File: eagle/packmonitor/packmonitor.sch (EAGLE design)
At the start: 29 parts, among them IC1 24C64, IC2 TCA4311A, IC3 AVRXDA32TQFP, IC4 ACS712

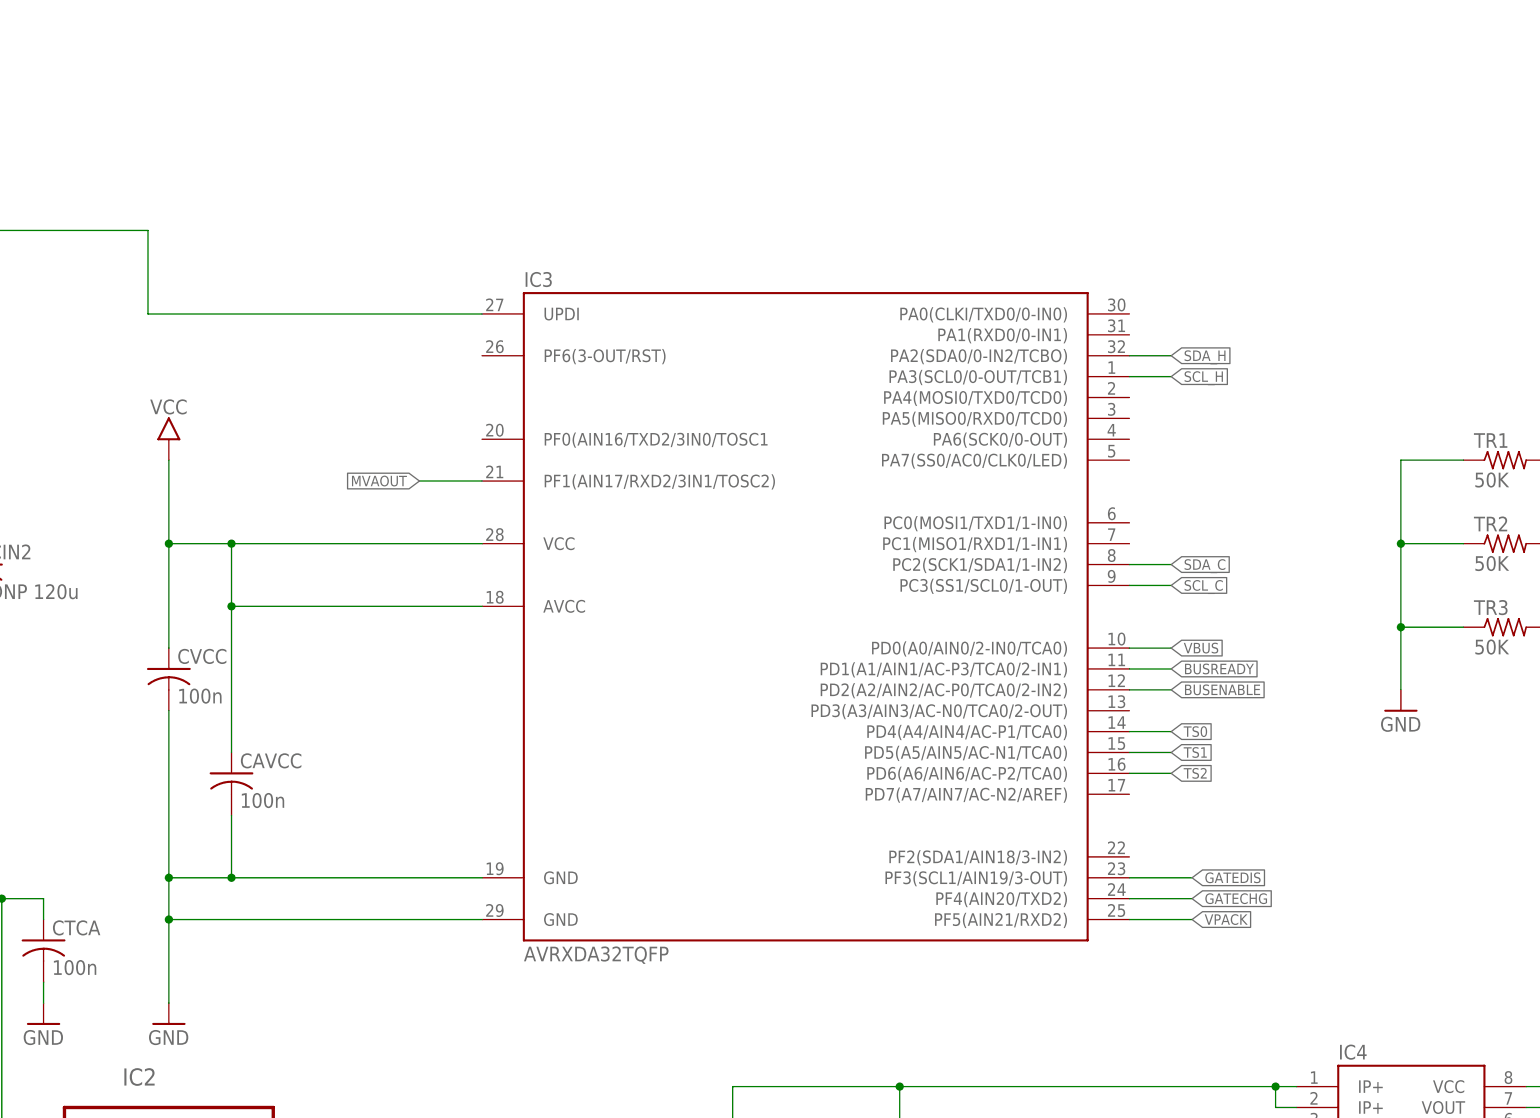
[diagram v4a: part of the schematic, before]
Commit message: Added pull up resistors on i2c busses
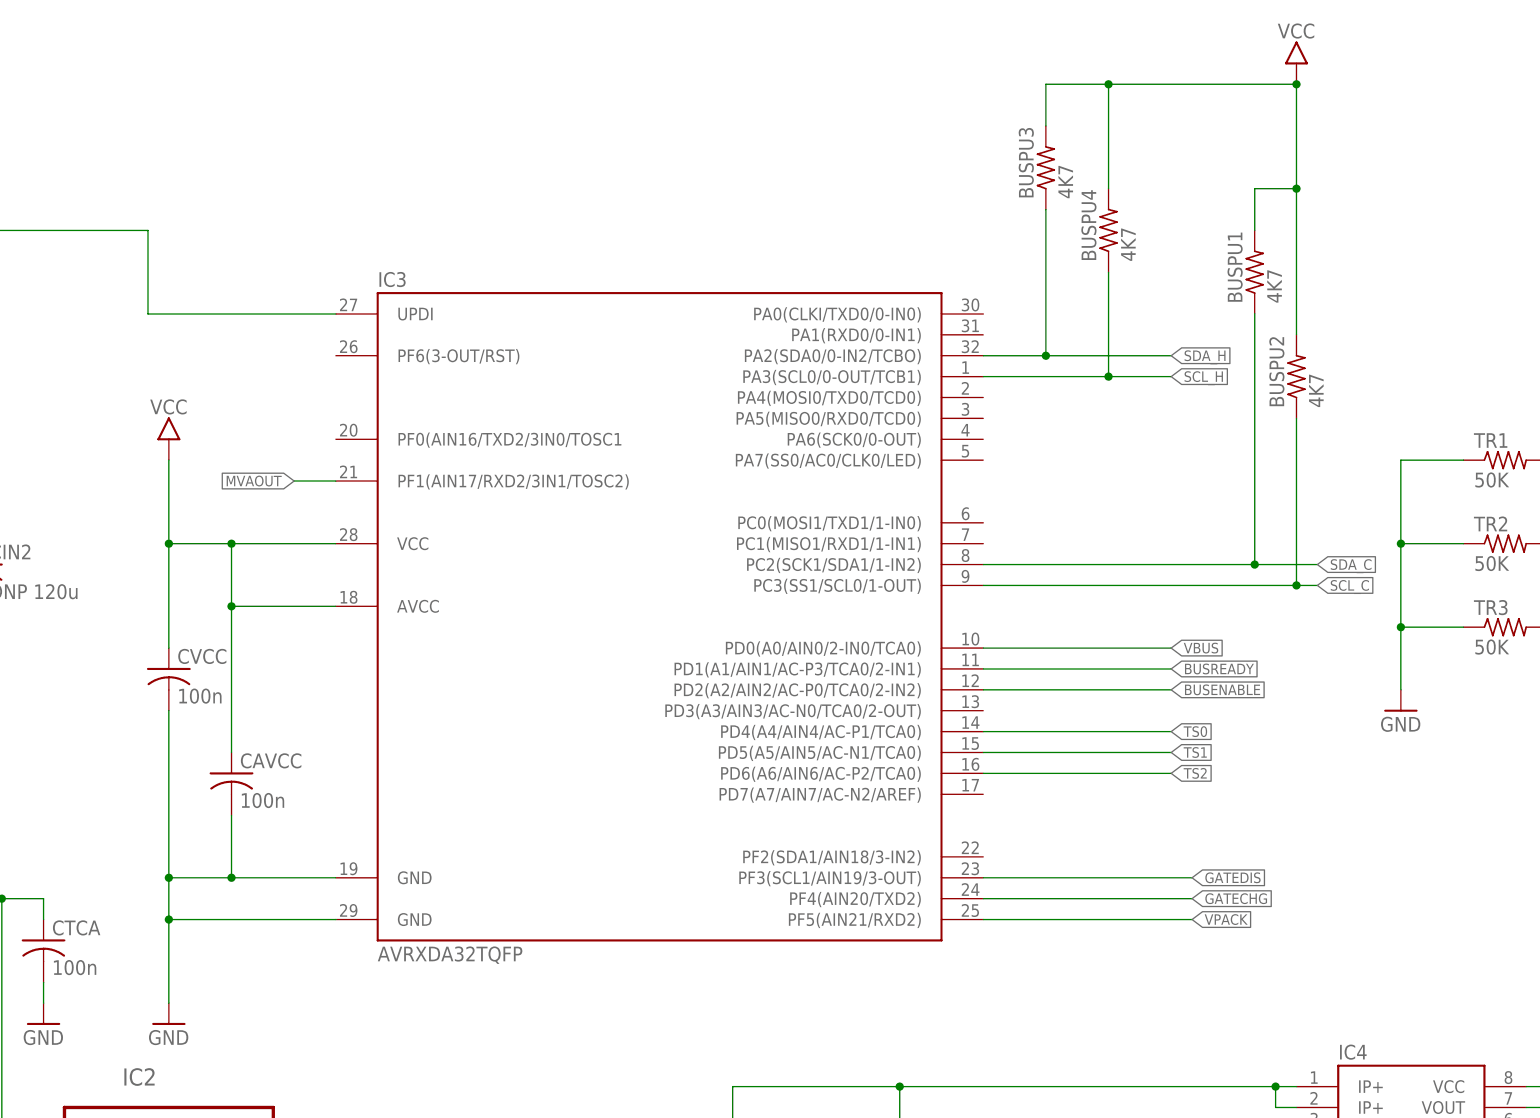
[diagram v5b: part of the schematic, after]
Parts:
- added BUSPU1, BUSPU2, BUSPU3, BUSPU4: 4K7, rcl:R-US_R0603
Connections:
- net SCL_C: now also BUSPU2.1
- net SCL_H: now also BUSPU4.1
- net SDA_C: now also BUSPU1.1
- net SDA_H: now also BUSPU3.1
- net VCC: now also BUSPU1.2, BUSPU2.2, BUSPU3.2, BUSPU4.2
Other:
- moved on the sheet: IC3
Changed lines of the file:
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@@
 <part name="RENA" library="rcl" deviceset="R-US_" device="R0603" value="10K"/>
 <part name="CACS1" library="rcl" deviceset="C-US" device="C0603" value="1n"/>
+<part name="BUSPU1" library="rcl" deviceset="R-US_" device="R0603" value="4K7"/>
+<part name="BUSPU2" library="rcl" deviceset="R-US_" device="R0603" value="4K7"/>
+<part name="U$4" library="bt" deviceset="VCC" device=""/>
+<part name="BUSPU3" library="rcl" deviceset="R-US_" device="R0603" value="4K7"/>
+<part name="BUSPU4" library="rcl" deviceset="R-US_" device="R0603" value="4K7"/>
 </parts>
 <sheets>
@@
 <instance part="CACS2" gate="G$1" x="180.34" y="88.9"/>
 <instance part="CIN1" gate="G$1" x="-45.72" y="154.94"/>
-<instance part="IC3" gate="G$1" x="71.12" y="147.32"/>
+<instance part="IC3" gate="G$1" x="53.34" y="147.32"/>
 <instance part="QCHG" gate="G$1" x="111.76" y="35.56" rot="R270"/>
 <instance part="QDIS" gate="G$1" x="127" y="35.56" rot="MR270"/>
@@
 <instance part="RENA" gate="G$1" x="-33.02" y="55.88" rot="R90"/>
 <instance part="CACS1" gate="G$1" x="172.72" y="73.66"/>
+<instance part="BUSPU1" gate="G$1" x="124.46" y="190.5" rot="R90"/>
+<instance part="BUSPU2" gate="G$1" x="129.54" y="177.8" rot="R90"/>
+<instance part="U$4" gate="G$1" x="129.54" y="213.36"/>
+<instance part="BUSPU3" gate="G$1" x="99.06" y="203.2" rot="R90"/>
+<instance part="BUSPU4" gate="G$1" x="106.68" y="195.58" rot="R90"/>
 </instances>
 <busses>
@@
 <segment>
 <pinref part="U$2" gate="G$1" pin="VCC"/>
-<wire x1="30.48" y1="157.48" x2="0" y2="157.48" width="0.1524" layer="91"/>
+<wire x1="12.7" y1="157.48" x2="0" y2="157.48" width="0.1524" layer="91"/>
 <wire x1="0" y1="157.48" x2="-7.62" y2="157.48" width="0.1524" layer="91"/>
 <wire x1="-7.62" y1="157.48" x2="-7.62" y2="167.64" width="0.1524" layer="91"/>
@@
 <junction x="-7.62" y="157.48"/>
 <pinref part="CAVCC" gate="G$1" pin="1"/>
-<wire x1="30.48" y1="149.86" x2="0" y2="149.86" width="0.1524" layer="91"/>
+<wire x1="12.7" y1="149.86" x2="0" y2="149.86" width="0.1524" layer="91"/>
 <wire x1="0" y1="149.86" x2="0" y2="132.08" width="0.1524" layer="91"/>
 <wire x1="0" y1="149.86" x2="0" y2="157.48" width="0.1524" layer="91"/>
@@
 <junction x="162.56" y="93.98"/>
 </segment>
+<segment>
+<pinref part="BUSPU2" gate="G$1" pin="2"/>
+<wire x1="129.54" y1="182.88" x2="129.54" y2="200.66" width="0.1524" layer="91"/>
+<pinref part="BUSPU1" gate="G$1" pin="2"/>
+<wire x1="129.54" y1="200.66" x2="124.46" y2="200.66" width="0.1524" layer="91"/>
+<wire x1="124.46" y1="200.66" x2="124.46" y2="195.58" width="0.1524" layer="91"/>
+<wire x1="129.54" y1="200.66" x2="129.54" y2="213.36" width="0.1524" layer="91"/>
+<junction x="129.54" y="200.66"/>
+<pinref part="U$4" gate="G$1" pin="VCC"/>
+<pinref part="BUSPU3" gate="G$1" pin="2"/>
+<wire x1="99.06" y1="208.28" x2="99.06" y2="213.36" width="0.1524" layer="91"/>
+<wire x1="99.06" y1="213.36" x2="106.68" y2="213.36" width="0.1524" layer="91"/>
+<junction x="129.54" y="213.36"/>
+<pinref part="BUSPU4" gate="G$1" pin="2"/>
+<wire x1="106.68" y1="213.36" x2="129.54" y2="213.36" width="0.1524" layer="91"/>
+<wire x1="106.68" y1="200.66" x2="106.68" y2="213.36" width="0.1524" layer="91"/>
+<junction x="106.68" y="213.36"/>
+</segment>
 </net>
 <net name="GND" class="0">
@@
 <wire x1="-7.62" y1="116.84" x2="-7.62" y2="111.76" width="0.1524" layer="91"/>
 <wire x1="-7.62" y1="111.76" x2="-7.62" y2="101.6" width="0.1524" layer="91"/>
-<wire x1="30.48" y1="111.76" x2="-7.62" y2="111.76" width="0.1524" layer="91"/>
-<wire x1="30.48" y1="116.84" x2="0" y2="116.84" width="0.1524" layer="91"/>
+<wire x1="12.7" y1="111.76" x2="-7.62" y2="111.76" width="0.1524" layer="91"/>
+<wire x1="12.7" y1="116.84" x2="0" y2="116.84" width="0.1524" layer="91"/>
 <junction x="-7.62" y="116.84"/>
 <junction x="-7.62" y="111.76"/>
@@
 <wire x1="-45.72" y1="195.58" x2="-10.16" y2="195.58" width="0.1524" layer="91"/>
 <wire x1="-10.16" y1="195.58" x2="-10.16" y2="185.42" width="0.1524" layer="91"/>
-<wire x1="-10.16" y1="185.42" x2="30.48" y2="185.42" width="0.1524" layer="91"/>
+<wire x1="-10.16" y1="185.42" x2="12.7" y2="185.42" width="0.1524" layer="91"/>
 <pinref part="IC3" gate="G$1" pin="UPDI"/>
 </segment>
@@
 <segment>
 <pinref part="IC3" gate="G$1" pin="PD2(A2/AIN2/AC-P0/TCA0/2-IN2)"/>
-<wire x1="114.3" y1="139.7" x2="109.22" y2="139.7" width="0.1524" layer="91"/>
+<wire x1="114.3" y1="139.7" x2="91.44" y2="139.7" width="0.1524" layer="91"/>
 <label x="114.3" y="139.7" size="1.27" layer="95" xref="yes"/>
 </segment>
@@
 <segment>
 <pinref part="IC3" gate="G$1" pin="PD1(A1/AIN1/AC-P3/TCA0/2-IN1)"/>
-<wire x1="114.3" y1="142.24" x2="109.22" y2="142.24" width="0.1524" layer="91"/>
+<wire x1="114.3" y1="142.24" x2="91.44" y2="142.24" width="0.1524" layer="91"/>
 <label x="114.3" y="142.24" size="1.27" layer="95" xref="yes"/>
 </segment>
@@
 <label x="114.3" y="144.78" size="1.27" layer="95" xref="yes"/>
 <pinref part="IC3" gate="G$1" pin="PD0(A0/AIN0/2-IN0/TCA0)"/>
-<wire x1="114.3" y1="144.78" x2="109.22" y2="144.78" width="0.1524" layer="91"/>
+<wire x1="114.3" y1="144.78" x2="91.44" y2="144.78" width="0.1524" layer="91"/>
 </segment>
 </net>
@@
 </segment>
 <segment>
-<wire x1="114.3" y1="134.62" x2="109.22" y2="134.62" width="0.1524" layer="91"/>
+<wire x1="114.3" y1="134.62" x2="91.44" y2="134.62" width="0.1524" layer="91"/>
 <label x="114.3" y="134.62" size="1.27" layer="95" xref="yes"/>
 <pinref part="IC3" gate="G$1" pin="PD4(A4/AIN4/AC-P1/TCA0)"/>
@@
 </segment>
 <segment>
-<wire x1="114.3" y1="132.08" x2="109.22" y2="132.08" width="0.1524" layer="91"/>
+<wire x1="114.3" y1="132.08" x2="91.44" y2="132.08" width="0.1524" layer="91"/>
 <label x="114.3" y="132.08" size="1.27" layer="95" xref="yes"/>
 <pinref part="IC3" gate="G$1" pin="PD5(A5/AIN5/AC-N1/TCA0)"/>
@@
 </segment>
 <segment>
-<wire x1="114.3" y1="129.54" x2="109.22" y2="129.54" width="0.1524" layer="91"/>
+<wire x1="114.3" y1="129.54" x2="91.44" y2="129.54" width="0.1524" layer="91"/>
 <label x="114.3" y="129.54" size="1.27" layer="95" xref="yes"/>
 <pinref part="IC3" gate="G$1" pin="PD6(A6/AIN6/AC-P2/TCA0)"/>
@@
 <segment>
 <pinref part="IC3" gate="G$1" pin="PF1(AIN17/RXD2/3IN1/TOSC2)"/>
-<wire x1="22.86" y1="165.1" x2="30.48" y2="165.1" width="0.1524" layer="91"/>
-<label x="22.86" y="165.1" size="1.27" layer="95" rot="R180" xref="yes"/>
+<wire x1="7.62" y1="165.1" x2="12.7" y2="165.1" width="0.1524" layer="91"/>
+<label x="7.62" y="165.1" size="1.27" layer="95" rot="R180" xref="yes"/>
 </segment>
 </net>
 <net name="SDA_H" class="0">
 <segment>
-<wire x1="114.3" y1="180.34" x2="109.22" y2="180.34" width="0.1524" layer="91"/>
+<wire x1="114.3" y1="180.34" x2="99.06" y2="180.34" width="0.1524" layer="91"/>
 <label x="114.3" y="180.34" size="1.27" layer="95" xref="yes"/>
 <pinref part="IC3" gate="G$1" pin="PA2(SDA0/0-IN2/TCBO)"/>
+<pinref part="BUSPU3" gate="G$1" pin="1"/>
+<wire x1="99.06" y1="180.34" x2="91.44" y2="180.34" width="0.1524" layer="91"/>
+<wire x1="99.06" y1="198.12" x2="99.06" y2="180.34" width="0.1524" layer="91"/>
+<junction x="99.06" y="180.34"/>
 </segment>
 <segment>
@@
 <net name="SCL_H" class="0">
 <segment>
-<wire x1="114.3" y1="177.8" x2="109.22" y2="177.8" width="0.1524" layer="91"/>
+<wire x1="114.3" y1="177.8" x2="106.68" y2="177.8" width="0.1524" layer="91"/>
 <label x="114.3" y="177.8" size="1.27" layer="95" xref="yes"/>
 <pinref part="IC3" gate="G$1" pin="PA3(SCL0/0-OUT/TCB1)"/>
+<pinref part="BUSPU4" gate="G$1" pin="1"/>
+<wire x1="106.68" y1="177.8" x2="91.44" y2="177.8" width="0.1524" layer="91"/>
+<wire x1="106.68" y1="190.5" x2="106.68" y2="177.8" width="0.1524" layer="91"/>
+<junction x="106.68" y="177.8"/>
 </segment>
 <segment>
@@
 <segment>
 <pinref part="IC3" gate="G$1" pin="PC2(SCK1/SDA1/1-IN2)"/>
-<wire x1="114.3" y1="154.94" x2="109.22" y2="154.94" width="0.1524" layer="91"/>
-<label x="114.3" y="154.94" size="1.27" layer="95" xref="yes"/>
+<wire x1="132.08" y1="154.94" x2="124.46" y2="154.94" width="0.1524" layer="91"/>
+<label x="132.08" y="154.94" size="1.27" layer="95" xref="yes"/>
+<pinref part="BUSPU1" gate="G$1" pin="1"/>
+<wire x1="124.46" y1="154.94" x2="91.44" y2="154.94" width="0.1524" layer="91"/>
+<wire x1="124.46" y1="154.94" x2="124.46" y2="185.42" width="0.1524" layer="91"/>
+<junction x="124.46" y="154.94"/>
 </segment>
 <segment>
@@
 <segment>
 <pinref part="IC3" gate="G$1" pin="PC3(SS1/SCL0/1-OUT)"/>
-<wire x1="114.3" y1="152.4" x2="109.22" y2="152.4" width="0.1524" layer="91"/>
-<label x="114.3" y="152.4" size="1.27" layer="95" xref="yes"/>
+<wire x1="132.08" y1="152.4" x2="129.54" y2="152.4" width="0.1524" layer="91"/>
+<label x="132.08" y="152.4" size="1.27" layer="95" xref="yes"/>
+<pinref part="BUSPU2" gate="G$1" pin="1"/>
+<wire x1="129.54" y1="152.4" x2="91.44" y2="152.4" width="0.1524" layer="91"/>
+<wire x1="129.54" y1="152.4" x2="129.54" y2="172.72" width="0.1524" layer="91"/>
+<junction x="129.54" y="152.4"/>
 </segment>
 <segment>
@@
 <segment>
 <pinref part="IC3" gate="G$1" pin="PF3(SCL1/AIN19/3-OUT)"/>
-<wire x1="116.84" y1="116.84" x2="109.22" y2="116.84" width="0.1524" layer="91"/>
+<wire x1="116.84" y1="116.84" x2="91.44" y2="116.84" width="0.1524" layer="91"/>
 <label x="116.84" y="116.84" size="1.27" layer="95" xref="yes"/>
 </segment>
@@
 <segment>
 <pinref part="IC3" gate="G$1" pin="PF4(AIN20/TXD2)"/>
-<wire x1="116.84" y1="114.3" x2="109.22" y2="114.3" width="0.1524" layer="91"/>
+<wire x1="116.84" y1="114.3" x2="91.44" y2="114.3" width="0.1524" layer="91"/>
 <label x="116.84" y="114.3" size="1.27" layer="95" xref="yes"/>
 </segment>
@@
 </segment>
 <segment>
-<wire x1="116.84" y1="111.76" x2="109.22" y2="111.76" width="0.1524" layer="91"/>
+<wire x1="116.84" y1="111.76" x2="91.44" y2="111.76" width="0.1524" layer="91"/>
 <label x="116.84" y="111.76" size="1.27" layer="95" xref="yes"/>
 <pinref part="IC3" gate="G$1" pin="PF5(AIN21/RXD2)"/>
